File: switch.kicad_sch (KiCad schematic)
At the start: 4 parts, among them Q48 Q_Photo_NPN

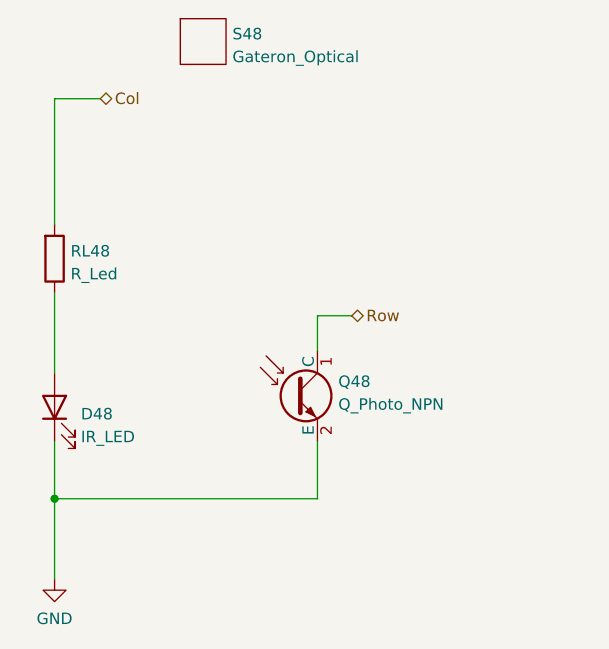
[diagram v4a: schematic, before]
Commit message: Add footprints library
A  OpticalSymbols_Library.kicad_sym
A  Optical_Parts.pretty/BlackPill_STLINK.kicad_mod
A  Optical_Parts.pretty/BlackPill_STLINK2.kicad_mod
A  Optical_Parts.pretty/Everlight_IR_IR12-21C_TR8.kicad_mod
A  Optical_Parts.pretty/Everlight_PT_PT12-21C_TR8.kicad_mod
A  Optical_Parts.pretty/Gateron_Optical_Switch.kicad_mod
A  Optical_Parts.pretty/Gateron_Switch_Basic.kicad_mod
A  Optical_Parts.pretty/MountingHole_1.2mm_M1.kicad_mod
A  Optical_Parts.pretty/MountingHole_2.2mm_M2.kicad_mod
A  Optical_Parts.pretty/MountingHole_2.2mm_M2_jlcpcb.kicad_mod
A  Optical_Parts.pretty/Switch_Cutout.kicad_mod
A  Optical_Parts.pretty/Switch_Cutout_1.25u.kicad_mod
A  Optical_Parts.pretty/Switch_Cutout_1.5u.kicad_mod
A  Optical_Parts.pretty/Switch_Cutout_1.75u.kicad_mod
A  Optical_Parts.pretty/TestPoint_Plated_Hole_D1.2mm.kicad_mod
A  Optical_Parts.pretty/TestPoint_THTPad_1.0x1.5mm_Drill0.5mm.kicad_mod
A  Optical_Parts.pretty/TestPoint_THTPad_1.0x2.5mm_Drill0.5mm.kicad_mod
M  README.md
M  fp-lib-table
M  optical-keyboard.kicad_pcb
M  switch.kicad_sch
M  sym-lib-table
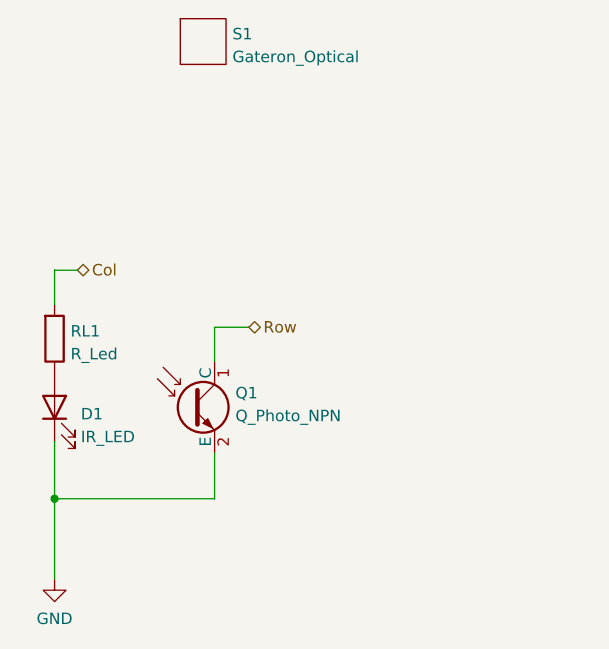
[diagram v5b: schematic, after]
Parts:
- renumbered D48 to D1, Q48 to Q1, RL48 to RL1, S48 to S1
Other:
- moved on the sheet: Q1, RL1
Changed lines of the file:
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@@
   (junction (at 116.84 110.49) (diameter 0) (color 0 0 0 0)
   )
-  (wire (pts (xy 146.05 104.14) (xy 146.05 110.49))
-    (stroke (width 0) (type default) (color 0 0 0 0))
-  )
-  (wire (pts (xy 146.05 110.49) (xy 116.84 110.49))
-    (stroke (width 0) (type default) (color 0 0 0 0))
-  )
-  (wire (pts (xy 116.84 66.04) (xy 116.84 80.01))
-    (stroke (width 0) (type default) (color 0 0 0 0))
-  )
-  (wire (pts (xy 146.05 90.17) (xy 149.86 90.17))
-    (stroke (width 0) (type default) (color 0 0 0 0))
-  )
-  (wire (pts (xy 116.84 110.49) (xy 116.84 104.14))
-    (stroke (width 0) (type default) (color 0 0 0 0))
-  )
-  (wire (pts (xy 116.84 66.04) (xy 121.92 66.04))
-    (stroke (width 0) (type default) (color 0 0 0 0))
-  )
-  (wire (pts (xy 146.05 90.17) (xy 146.05 93.98))
-    (stroke (width 0) (type default) (color 0 0 0 0))
-  )
-  (wire (pts (xy 116.84 87.63) (xy 116.84 96.52))
+  (wire (pts (xy 116.84 88.9) (xy 116.84 85.09))
     (stroke (width 0) (type default) (color 0 0 0 0))
   )
@@
     (stroke (width 0) (type default) (color 0 0 0 0))
   )
-  (hierarchical_label "Col" (shape bidirectional) (at 121.92 66.04 0)
+  (wire (pts (xy 134.62 91.44) (xy 138.43 91.44))
+    (stroke (width 0) (type default) (color 0 0 0 0))
+  )
+  (wire (pts (xy 116.84 104.14) (xy 116.84 110.49))
+    (stroke (width 0) (type default) (color 0 0 0 0))
+  )
+  (wire (pts (xy 116.84 85.09) (xy 119.38 85.09))
+    (stroke (width 0) (type default) (color 0 0 0 0))
+  )
+  (wire (pts (xy 134.62 91.44) (xy 134.62 95.25))
+    (stroke (width 0) (type default) (color 0 0 0 0))
+  )
+  (wire (pts (xy 134.62 110.49) (xy 116.84 110.49))
+    (stroke (width 0) (type default) (color 0 0 0 0))
+  )
+  (wire (pts (xy 134.62 105.41) (xy 134.62 110.49))
+    (stroke (width 0) (type default) (color 0 0 0 0))
+  )
+  (hierarchical_label "Col" (shape bidirectional) (at 119.38 85.09 0)
     (effects (font (size 1.27 1.27)) (justify left))
   )
-  (hierarchical_label "Row" (shape bidirectional) (at 149.86 90.17 0)
+  (hierarchical_label "Row" (shape bidirectional) (at 138.43 91.44 0)
     (effects (font (size 1.27 1.27)) (justify left))
   )
   (symbol (lib_id "OpticalParts:IR_LED") (at 116.84 100.33 90)
     (in_bom yes) (on_board yes) (fields_autoplaced)
-    (property "Reference" "D48" (id 0) (at 119.761 101.0828 90)
+    (property "Reference" "D1" (id 0) (at 119.761 101.0828 90)
       (effects (font (size 1.27 1.27)) (justify right))
     )
@@
     (pin "2")
   )
-  (symbol (lib_id "OpticalParts:Q_Photo_NPN") (at 143.51 99.06 0)
+  (symbol (lib_id "OpticalParts:Q_Photo_NPN") (at 132.08 100.33 0)
     (in_bom yes) (on_board yes) (fields_autoplaced)
-    (property "Reference" "Q48" (id 0) (at 148.3614 97.476 0)
+    (property "Reference" "Q1" (id 0) (at 136.9314 98.746 0)
       (effects (font (size 1.27 1.27)) (justify left))
     )
-    (property "Value" "Q_Photo_NPN" (id 1) (at 148.3614 100.0129 0)
+    (property "Value" "Q_Photo_NPN" (id 1) (at 136.9314 101.2829 0)
       (effects (font (size 1.27 1.27)) (justify left))
     )
-    (property "Footprint" "OpticalParts:Everlight_PT_PT12-21C_TR8" (id 2) (at 148.59 96.52 0)
+    (property "Footprint" "OpticalParts:Everlight_PT_PT12-21C_TR8" (id 2) (at 137.16 97.79 0)
       (effects (font (size 1.27 1.27)) hide)
     )
-    (property "Datasheet" "~" (id 3) (at 143.51 99.06 0)
+    (property "Datasheet" "~" (id 3) (at 132.08 100.33 0)
       (effects (font (size 1.27 1.27)) hide)
     )
-    (property "JLC" "SMD_1.0x3.0x2.0" (id 4) (at 140.97 104.14 0)
+    (property "JLC" "SMD_1.0x3.0x2.0" (id 4) (at 129.54 105.41 0)
       (effects (font (size 0.5 0.5)) hide)
     )
-    (property "LCSC" "C264383" (id 5) (at 142.24 93.98 0)
+    (property "LCSC" "C264383" (id 5) (at 130.81 95.25 0)
       (effects (font (size 0.5 0.5)) hide)
     )
@@
   (symbol (lib_id "OpticalParts:Gateron_Optical") (at 133.35 59.69 0)
     (in_bom yes) (on_board yes) (fields_autoplaced)
-    (property "Reference" "S48" (id 0) (at 136.6012 58.8553 0)
+    (property "Reference" "S1" (id 0) (at 136.6012 58.8553 0)
       (effects (font (size 1.27 1.27)) (justify left))
     )
@@
     )
   )
-  (symbol (lib_id "OpticalParts:R_Led") (at 116.84 83.82 0)
+  (symbol (lib_id "OpticalParts:R_Led") (at 116.84 92.71 0)
     (in_bom yes) (on_board yes) (fields_autoplaced)
-    (property "Reference" "RL48" (id 0) (at 118.618 82.9853 0)
+    (property "Reference" "RL1" (id 0) (at 118.618 91.8753 0)
       (effects (font (size 1.27 1.27)) (justify left))
     )
-    (property "Value" "R_Led" (id 1) (at 118.618 85.5222 0)
+    (property "Value" "R_Led" (id 1) (at 118.618 94.4122 0)
       (effects (font (size 1.27 1.27)) (justify left))
     )
-    (property "Footprint" "Resistor_SMD:R_0603_1608Metric" (id 2) (at 118.11 90.17 90)
+    (property "Footprint" "Resistor_SMD:R_0603_1608Metric" (id 2) (at 118.11 99.06 90)
       (effects (font (size 1.27 1.27)) (justify left) hide)
     )
-    (property "Datasheet" "~" (id 3) (at 116.84 85.09 0)
+    (property "Datasheet" "~" (id 3) (at 116.84 93.98 0)
       (effects (font (size 1.27 1.27)) hide)
     )
-    (property "JLC" "0603-1608" (id 4) (at 120.65 87.63 0)
+    (property "JLC" "0603-1608" (id 4) (at 120.65 96.52 0)
       (effects (font (size 0.5 0.5)) hide)
     )
-    (property "LCSC" "C4190" (id 5) (at 120.65 80.01 0)
+    (property "LCSC" "C4190" (id 5) (at 120.65 88.9 0)
       (effects (font (size 0.5 0.5)) hide)
     )
@@
   (symbol (lib_id "power:GND") (at 116.84 119.38 0)
     (in_bom yes) (on_board yes) (fields_autoplaced)
-    (property "Reference" "#PWR078" (id 0) (at 116.84 125.73 0)
+    (property "Reference" "#PWR04" (id 0) (at 116.84 125.73 0)
       (effects (font (size 1.27 1.27)) hide)
     )
